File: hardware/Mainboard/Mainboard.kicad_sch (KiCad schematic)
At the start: 15 parts, among them CN1 NUCLE_F446RE_MORPHO_CN7, CN2 NUCLE_F446RE_MORPHO_CN10, J1 Conn_01x03_Pin, J2 Conn_01x03_Pin, J27 Conn_01x03_Pin, J29 Conn_01x02_Pin, J30 Conn_01x02_Pin, J4 Conn_01x02_Pin, J5 Conn_01x02_Pin

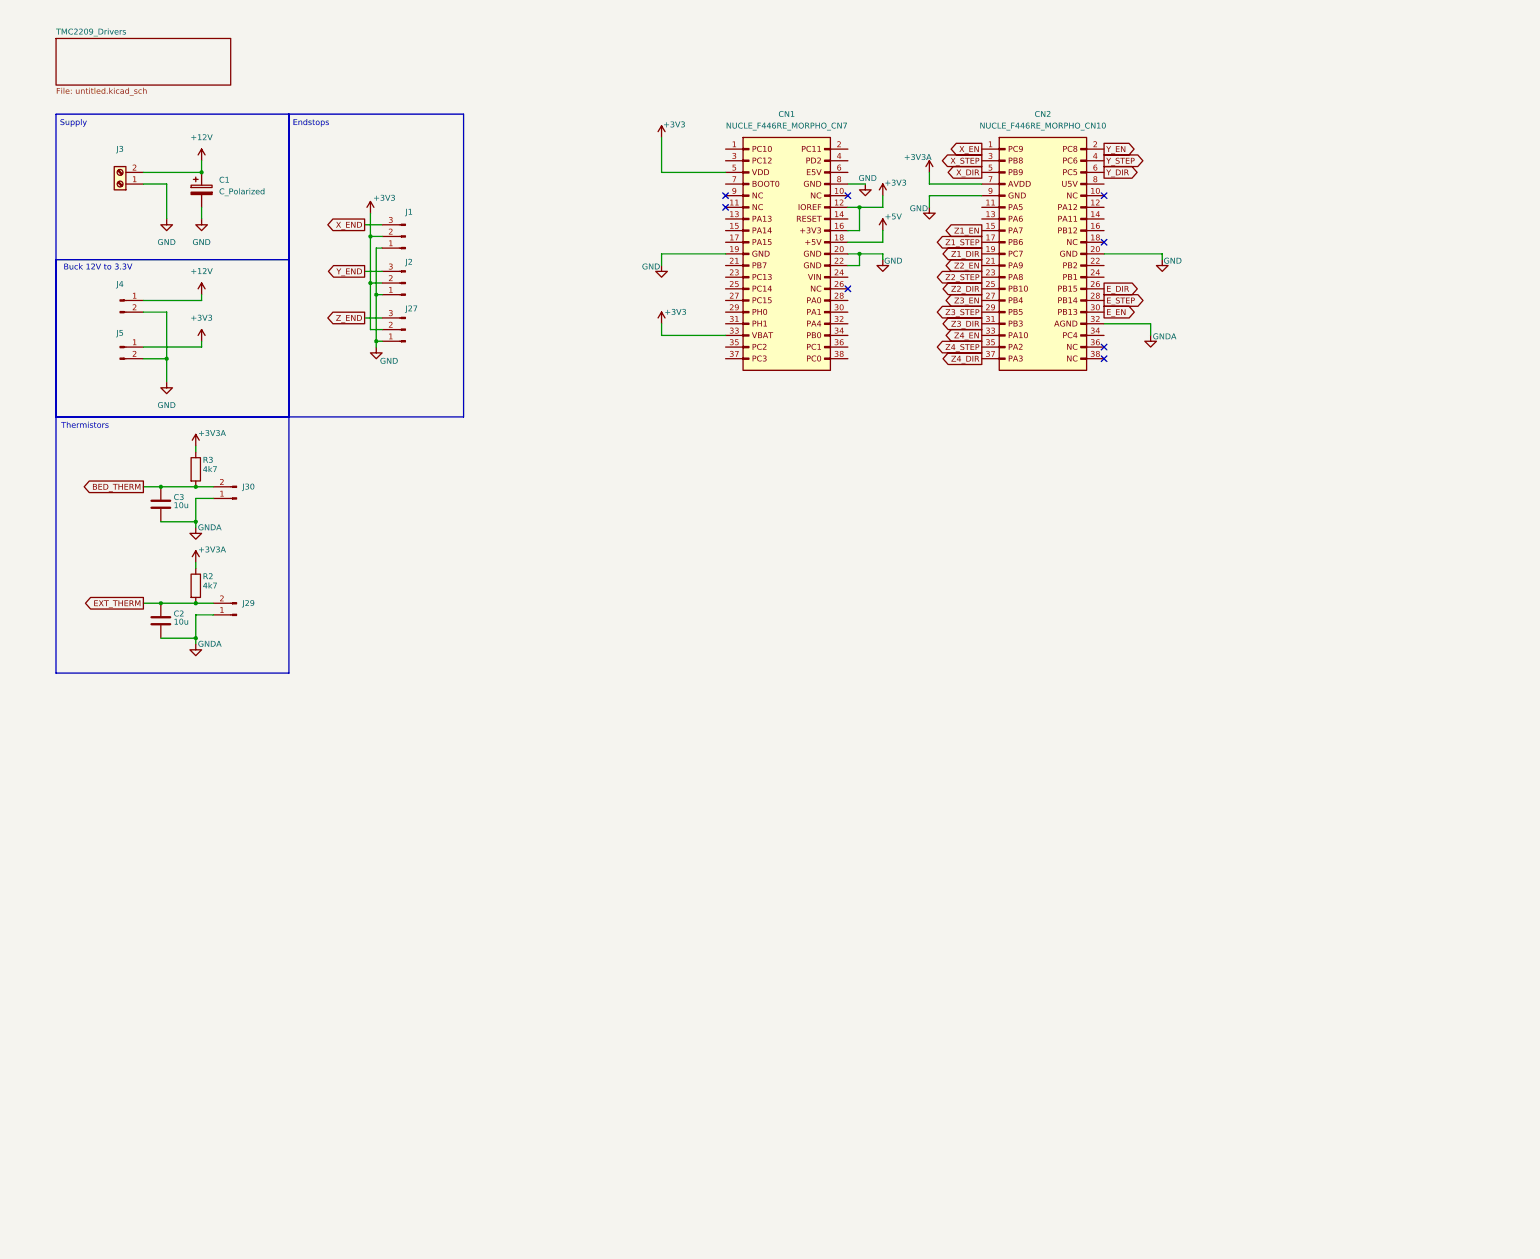
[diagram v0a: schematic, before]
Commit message: driver board finalized, mainboard started placing FET drivers
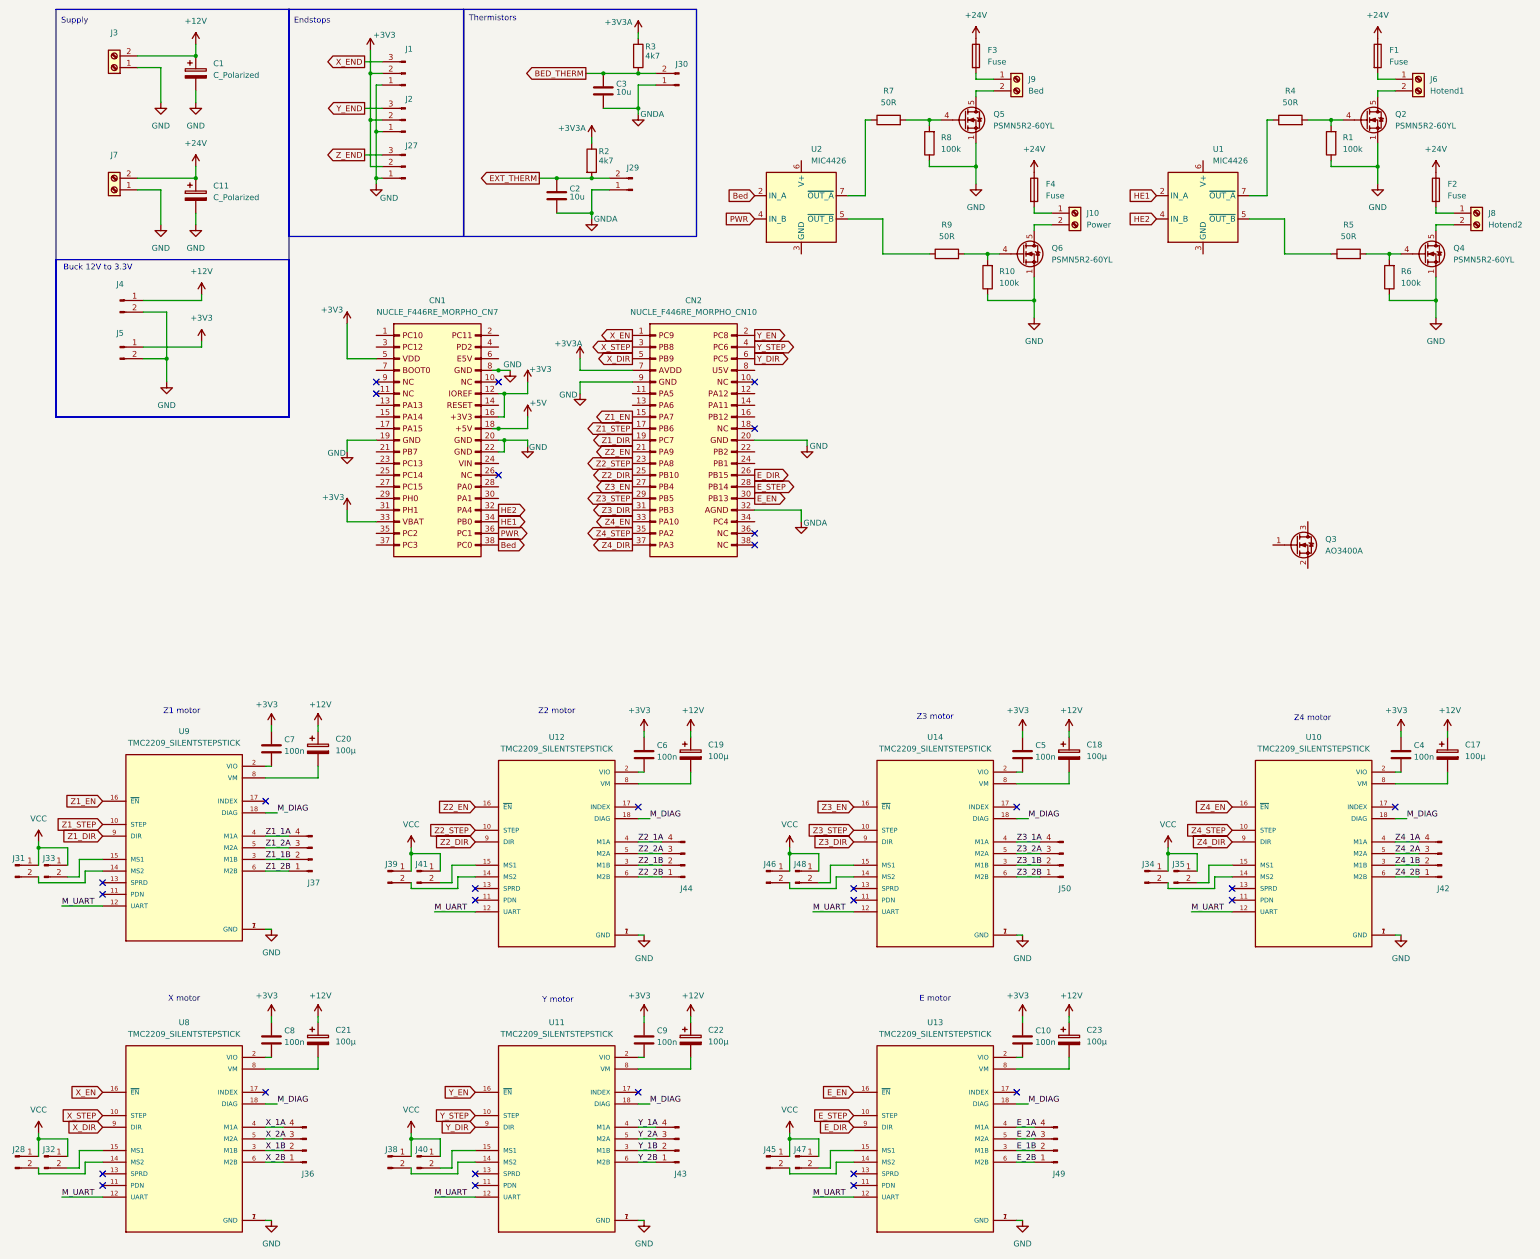
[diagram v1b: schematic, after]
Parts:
- added C10, C4, C5, C6, C7, C8, C9: 100n, symbol Device:C
- added C11: C_Polarized, symbol Device:C_Polarized
- added C17, C18, C19, C20, C21, C22, C23: 100µ, symbol Device:C_Polarized
- added F1, F2, F3, F4: Fuse, symbol Device:Fuse
- added J10: Power, symbol Connector:Screw_Terminal_01x02
- added J28, J31, J32, J33, J34, J35, J38, J39, J40, J41, J45, J46, J47, J48: Conn_01x02_Pin, symbol Connector:Conn_01x02_Pin
- added J36, J37, J42, J43, J44, J49, J50: Conn_01x04_Pin, symbol Connector:Conn_01x04_Pin
- added J6: Hotend1, symbol Connector:Screw_Terminal_01x02
- added J7: ~, symbol Connector:Screw_Terminal_01x02
- added J8: Hotend2, symbol Connector:Screw_Terminal_01x02
- added J9: Bed, symbol Connector:Screw_Terminal_01x02
- added Q2, Q4, Q5, Q6: PSMN5R2-60YL, Package_TO_SOT_SMD:LFPAK56, symbol Transistor_FET:PSMN5R2-60YL
- added Q3: AO3400A, Package_TO_SOT_SMD:SOT-23, symbol Transistor_FET:AO3400A
- added R1, R10, R6, R8: 100k, symbol Device:R
- added R4, R5, R7, R9: 50R, symbol Device:R
- added U1, U2: MIC4426, symbol Driver_FET:MIC4426
- added U10, U11, U12, U13, U14, U8, U9: TMC2209_SILENTSTEPSTICK, symbol PacFab:TMC2209_SILENTSTEPSTICK
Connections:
- net +12V: now also C17.1, C18.1, C19.1, C20.1, C21.1, C22.1, C23.1
- net +3V3: now also C10.1, C4.1, C5.1, C6.1, C7.1, C8.1, C9.1
- net E_DIR: now also U13.9 (DIR)
- net E_EN: now also U13.16 (~{EN})
- net E_STEP: now also U13.10 (STEP)
- net GND: now also C11.2, J7.1 (Pin_1), Q2.1 (S), Q2.2 (S), Q2.3 (S), Q4.1 (S), Q4.2 (S), Q4.3 (S), Q5.1 (S), Q5.2 (S), Q5.3 (S), Q6.1 (S), Q6.2 (S), Q6.3 (S), R1.1, R10.1, R6.1, R8.1, U10.1 (GND), U10.7 (GND), U11.1 (GND), U11.7 (GND), U12.1 (GND), U12.7 (GND), U13.1 (GND), U13.7 (GND), U14.1 (GND), U14.7 (GND), U8.1 (GND), U8.7 (GND), U9.1 (GND), U9.7 (GND)
- net X_DIR: now also U8.9 (DIR)
- net X_EN: now also U8.16 (~{EN})
- net X_STEP: now also U8.10 (STEP)
- net Y_DIR: now also U11.9 (DIR)
- net Y_EN: now also U11.16 (~{EN})
- net Y_STEP: now also U11.10 (STEP)
- net Z1_DIR: now also U9.9 (DIR)
- net Z1_EN: now also U9.16 (~{EN})
- net Z1_STEP: now also U9.10 (STEP)
- net Z2_DIR: now also U12.9 (DIR)
- net Z2_EN: now also U12.16 (~{EN})
- net Z2_STEP: now also U12.10 (STEP)
- net Z3_DIR: now also U14.9 (DIR)
- net Z3_EN: now also U14.16 (~{EN})
- net Z3_STEP: now also U14.10 (STEP)
- net Z4_DIR: now also U10.9 (DIR)
- net Z4_EN: now also U10.16 (~{EN})
- net Z4_STEP: now also U10.10 (STEP)
- net HE2: now reaches CN1.32 (Pin_32)
- net HE2: now also U1.4 (IN_B)
- net HE1: now reaches CN1.34 (Pin_34)
- net HE1: now also U1.2 (IN_A)
- net PWR: now reaches CN1.36 (Pin_36)
- net PWR: now also U2.4 (IN_B)
- net Bed: now reaches CN1.38 (Pin_38)
- net Bed: now also U2.2 (IN_A)
- new net: J46.2 (Pin_2), U14.14 (MS2)
- new net: J48.2 (Pin_2), U14.15 (MS1)
- new net: C5.2, U14.2 (VIO)
- new net: C18.2, U14.8 (VM)
- new net: Q2.4 (G), R1.2, R4.2
- new net: J6.2 (Pin_2), Q2.5 (D)
- new net: C9.2, U11.2 (VIO)
- new net: F3.2, J9.1 (Pin_1)
- new net: R9.1, U2.5 (~{OUT_B})
- new net: R7.1, U2.7 (~{OUT_A})
- new net: C8.2, U8.2 (VIO)
- new net: J32.2 (Pin_2), U8.15 (MS1)
- new net: J47.2 (Pin_2), U13.15 (MS1)
- new net: Q4.4 (G), R5.2, R6.2
- new net: C7.2, U9.2 (VIO)
- new net: C23.2, U13.8 (VM)
- new net: C10.2, U13.2 (VIO)
- new net: F2.2, J8.1 (Pin_1)
- new net: Q5.4 (G), R7.2, R8.2
- new net: J9.2 (Pin_2), Q5.5 (D)
- new net: J35.2 (Pin_2), U10.15 (MS1)
- new net: C21.2, U8.8 (VM)
- new net: R5.1, U1.5 (~{OUT_B})
- new net: J39.2 (Pin_2), U12.14 (MS2)
- new net: Q6.4 (G), R10.2, R9.2
- new net: J33.2 (Pin_2), U9.15 (MS1)
- new net: J38.2 (Pin_2), U11.14 (MS2)
- new net: J34.2 (Pin_2), U10.14 (MS2)
- new net: C4.2, U10.2 (VIO)
- new net: C17.2, U10.8 (VM)
- new net: J41.2 (Pin_2), U12.15 (MS1)
- new net: C6.2, U12.2 (VIO)
- new net: C19.2, U12.8 (VM)
- new net: J45.2 (Pin_2), U13.14 (MS2)
- new net: J31.2 (Pin_2), U9.14 (MS2)
- new net: C20.2, U9.8 (VM)
- new net: J28.2 (Pin_2), U8.14 (MS2)
- new net: J8.2 (Pin_2), Q4.5 (D)
- new net: J40.2 (Pin_2), U11.15 (MS1)
- new net: C22.2, U11.8 (VM)
- new net: F1.2, J6.1 (Pin_1)
- new net: F4.2, J10.1 (Pin_1)
- new net: J10.2 (Pin_2), Q6.5 (D)
- new net: R4.1, U1.7 (~{OUT_A})
- new net +24V: C11.1, F1.1, F2.1, F3.1, F4.1, J7.2 (Pin_2)
- new net E_1A: J49.4 (Pin_4), U13.4 (M1A)
- new net E_1B: J49.2 (Pin_2), U13.3 (M1B)
- new net E_2A: J49.3 (Pin_3), U13.5 (M2A)
- new net E_2B: J49.1 (Pin_1), U13.6 (M2B)
- new net M_DIAG: U10.18 (DIAG), U11.18 (DIAG), U12.18 (DIAG), U13.18 (DIAG), U14.18 (DIAG), U8.18 (DIAG), U9.18 (DIAG)
- new net M_UART: U10.12 (UART), U11.12 (UART), U12.12 (UART), U13.12 (UART), U14.12 (UART), U8.12 (UART), U9.12 (UART)
- new net VCC: J28.1 (Pin_1), J31.1 (Pin_1), J32.1 (Pin_1), J33.1 (Pin_1), J34.1 (Pin_1), J35.1 (Pin_1), J38.1 (Pin_1), J39.1 (Pin_1), J40.1 (Pin_1), J41.1 (Pin_1), J45.1 (Pin_1), J46.1 (Pin_1), J47.1 (Pin_1), J48.1 (Pin_1)
- new net X_1A: J36.4 (Pin_4), U8.4 (M1A)
- new net X_1B: J36.2 (Pin_2), U8.3 (M1B)
- new net X_2A: J36.3 (Pin_3), U8.5 (M2A)
- new net X_2B: J36.1 (Pin_1), U8.6 (M2B)
- new net Y_1A: J43.4 (Pin_4), U11.4 (M1A)
- new net Y_1B: J43.2 (Pin_2), U11.3 (M1B)
- new net Y_2A: J43.3 (Pin_3), U11.5 (M2A)
- new net Y_2B: J43.1 (Pin_1), U11.6 (M2B)
- new net Z1_1A: J37.4 (Pin_4), U9.4 (M1A)
- new net Z1_1B: J37.2 (Pin_2), U9.3 (M1B)
- new net Z1_2A: J37.3 (Pin_3), U9.5 (M2A)
- new net Z1_2B: J37.1 (Pin_1), U9.6 (M2B)
- new net Z2_1A: J44.4 (Pin_4), U12.4 (M1A)
- new net Z2_1B: J44.2 (Pin_2), U12.3 (M1B)
- new net Z2_2A: J44.3 (Pin_3), U12.5 (M2A)
- new net Z2_2B: J44.1 (Pin_1), U12.6 (M2B)
- new net Z3_1A: J50.4 (Pin_4), U14.4 (M1A)
- new net Z3_1B: J50.2 (Pin_2), U14.3 (M1B)
- new net Z3_2A: J50.3 (Pin_3), U14.5 (M2A)
- new net Z3_2B: J50.1 (Pin_1), U14.6 (M2B)
- new net Z4_1A: J42.4 (Pin_4), U10.4 (M1A)
- new net Z4_1B: J42.2 (Pin_2), U10.3 (M1B)
- new net Z4_2A: J42.3 (Pin_3), U10.5 (M2A)
- new net Z4_2B: J42.1 (Pin_1), U10.6 (M2B)
- no-connect marks 8 -> 29
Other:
- removed sheet TMC2209_Drivers
- note added: "E motor"
- note added: "X motor"
- note added: "Y motor"
- note added: "Z1 motor"
- note added: "Z2 motor"
- note added: "Z3 motor"
- note added: "Z4 motor"
- moved on the sheet: C1, C2, C3, CN1, CN2, J1, J2, J27, J29, J3, J30, R2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

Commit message: Update Mainboard.kicad_sch
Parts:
- removed Q3: AO3400A, Package_TO_SOT_SMD:SOT-23, symbol Transistor_FET:AO3400A
- added J12: Part_Cooling2, symbol Connector:Screw_Terminal_01x02
- added J13: Part_Cooling1, symbol Connector:Screw_Terminal_01x02
- added Q7, Q8: AO3400A, Package_TO_SOT_SMD:SOT-23, symbol Transistor_FET:AO3400A
- added R15, R17: 100R, symbol Device:R
- added R16, R18: 100k, symbol Device:R
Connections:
- net +12V: now also J12.1 (Pin_1), J13.1 (Pin_1)
- net GND: now also Q7.2 (S), Q8.2 (S), R16.1, R18.1
- net PCF2: now reaches CN1.28 (Pin_28)
- net PCF2: now also R15.1
- net PCF1: now reaches CN1.30 (Pin_30)
- net PCF1: now also R17.1
- new net: Q7.1 (G), R15.2, R16.2
- new net: Q8.1 (G), R17.2, R18.2
- new net: J12.2 (Pin_2), Q7.3 (D)
- new net: J13.2 (Pin_2), Q8.3 (D)
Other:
- moved on the sheet: CN1, CN2

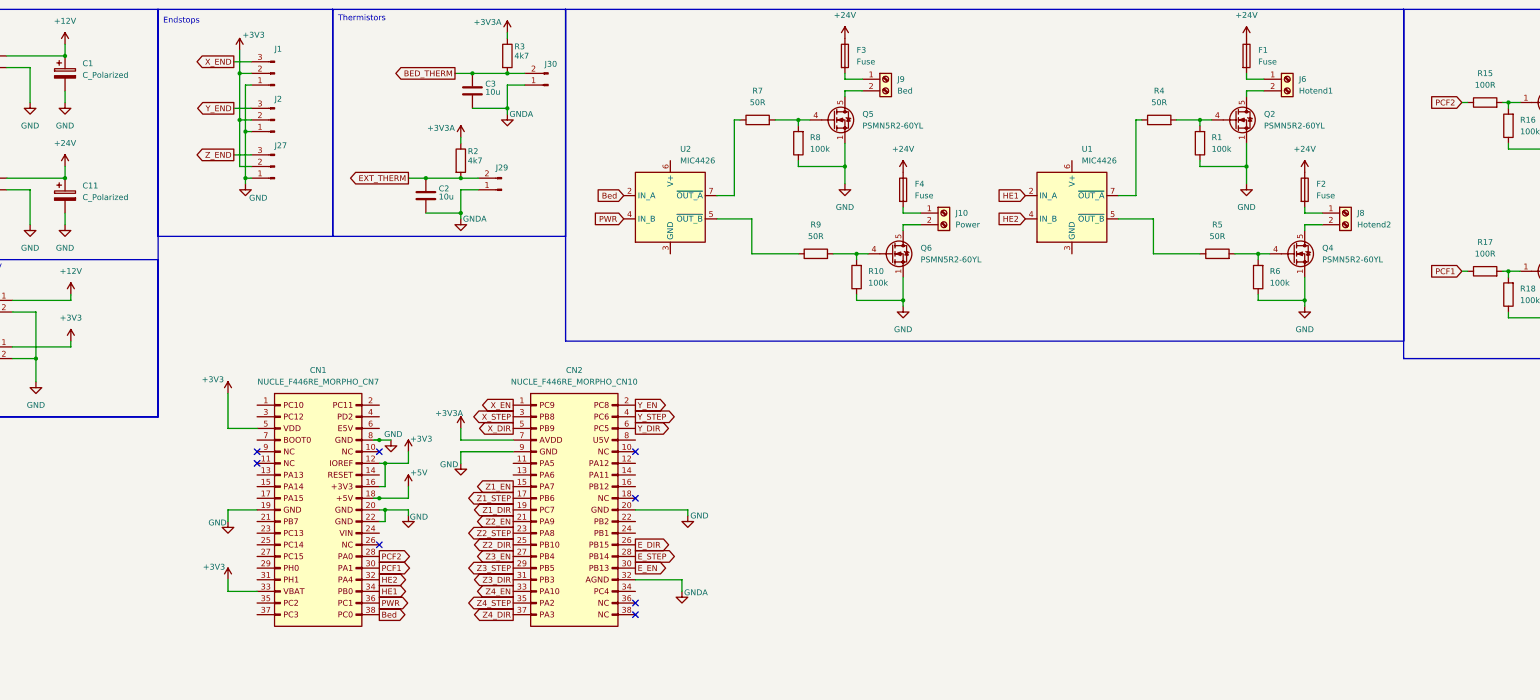
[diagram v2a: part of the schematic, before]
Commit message: Mainboard changes + BOM for Driver
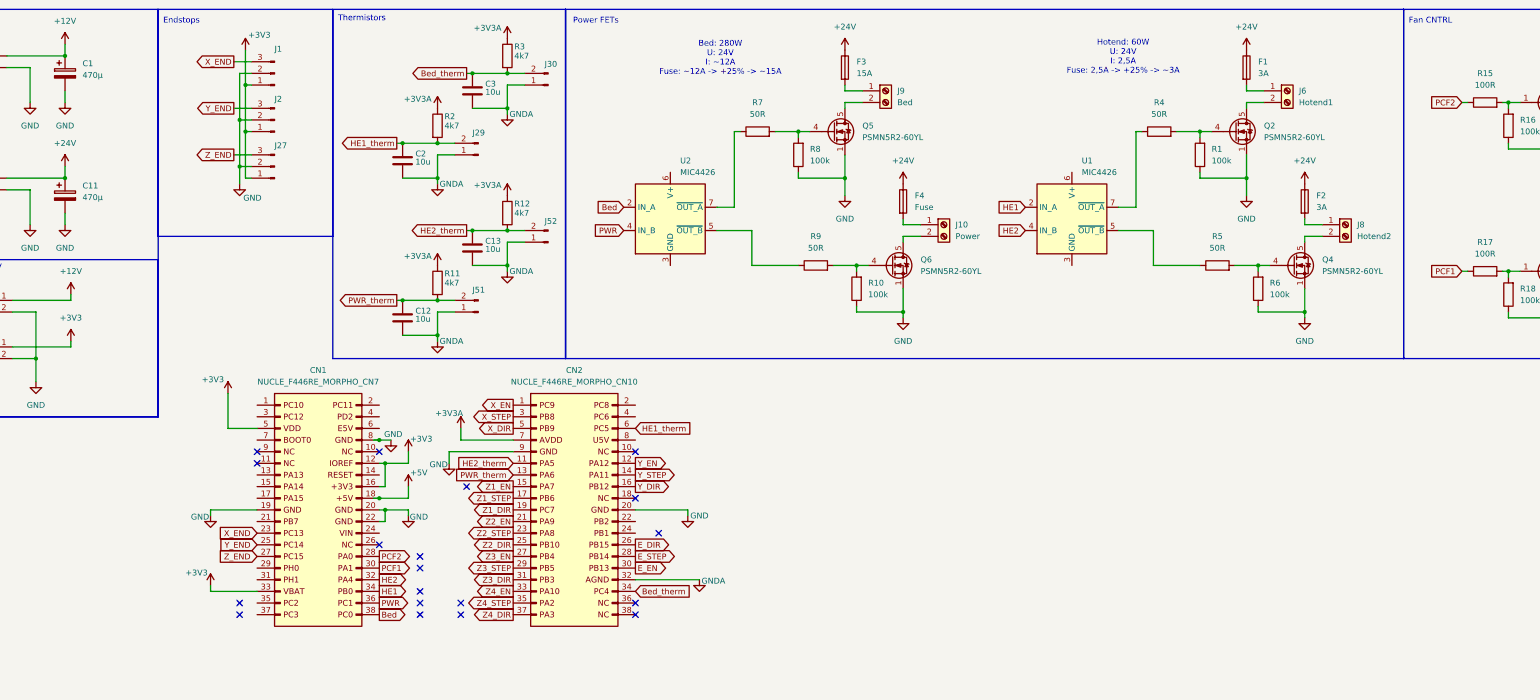
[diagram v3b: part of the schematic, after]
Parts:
- added C12, C13: 10u, Capacitor_SMD:C_0805_2012Metric, symbol Device:C
- added J51, J52: Conn_01x02_Pin, symbol Connector:Conn_01x02_Pin
- added R11, R12: 4k7, Resistor_SMD:R_0805_2012Metric, symbol Device:R
- C1, C11: value C_Polarized -> 470µ; footprint (none) -> Capacitor_SMD:CP_Elec_16x17.5
- C10, C2, C3, C4, C5, C6, C7, C8, C9: footprint (none) -> Capacitor_SMD:C_0805_2012Metric
- C17, C18, C19, C20, C21, C22, C23: footprint (none) -> Capacitor_SMD:CP_Elec_8x10
- F1, F2: value Fuse -> 3A
- F3: value Fuse -> 15A
- R1, R10, R15, R16, R17, R18, R2, R3, R4, R5, R6, R7, R8, R9: footprint (none) -> Resistor_SMD:R_0805_2012Metric
- U10: footprint (none) -> FlexPrint:MODULE_TMC2209_SILENTSTEPSTICK
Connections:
- net BED_THERM is gone; now on net Bed_therm: C3.1, J30.2 (Pin_2), R3.2
- net +3V3: now also J1.1 (Pin_1), J2.1 (Pin_1), J27.1 (Pin_1); no longer J1.2 (Pin_2), J2.2 (Pin_2), J27.2 (Pin_2)
- net +3V3A: now also R11.1, R12.1
- net GND: now also J1.2 (Pin_2), J2.2 (Pin_2), J27.2 (Pin_2); no longer J1.1 (Pin_1), J2.1 (Pin_1), J27.1 (Pin_1)
- net GNDA: now also C12.2, C13.2, J51.1 (Pin_1), J52.1 (Pin_1)
- net X_END: now also CN1.23 (Pin_23)
- net Y_DIR: now also CN2.16 (Pin_16); no longer CN2.6 (Pin_6)
- net Y_EN: now also CN2.12 (Pin_12); no longer CN2.2 (Pin_2)
- net Y_END: now also CN1.25 (Pin_25)
- net Y_STEP: now also CN2.14 (Pin_14); no longer CN2.4 (Pin_4)
- net Z_END: now also CN1.27 (Pin_27)
- net HE2_therm: now reaches CN2.11 (Pin_11)
- net HE2_therm: now also C13.1, J52.2 (Pin_2), R12.2
- net PWR_therm: now reaches CN2.13 (Pin_13)
- net PWR_therm: now also C12.1, J51.2 (Pin_2), R11.2
- net Bed_therm: now reaches CN2.34 (Pin_34)
- net EXT_THERM renamed HE1_therm
- net HE1_therm: now also CN2.6 (Pin_6)
- no-connect marks 29 -> 40
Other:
- note added: "Bed: 280W U: 24V I: ~12A Fuse: ~12A -> +25% -> ~15A"
- note added: "Fan CNTRL"
- note added: "Hotend: 60W U: 24V I: 2,5A Fuse: 2,5A -> +25% -> ~3A"
- note added: "Power FETs"
- moved on the sheet: C2, F1, F2, F3, F4, J10, J29, J6, J8, J9, Q2, Q4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
